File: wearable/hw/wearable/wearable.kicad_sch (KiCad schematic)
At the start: 104 parts, among them IC1 LM4041CILPR, J2 Conn_02x05_Odd_Even, J3 Interrupts, J4 Data, J5 Data, J8 USBC Charger, SW1 SW_Toggle, U1 LT3042xMSE, U2 BNO080, U3 nRF54L15-QFXX, U4 MAX77659AENV+, U5 ADS1299IPAG, U6 nPM1300-QEXX, Y1 32MHz, Y2 32.768kHz, Y3 32.768kHz

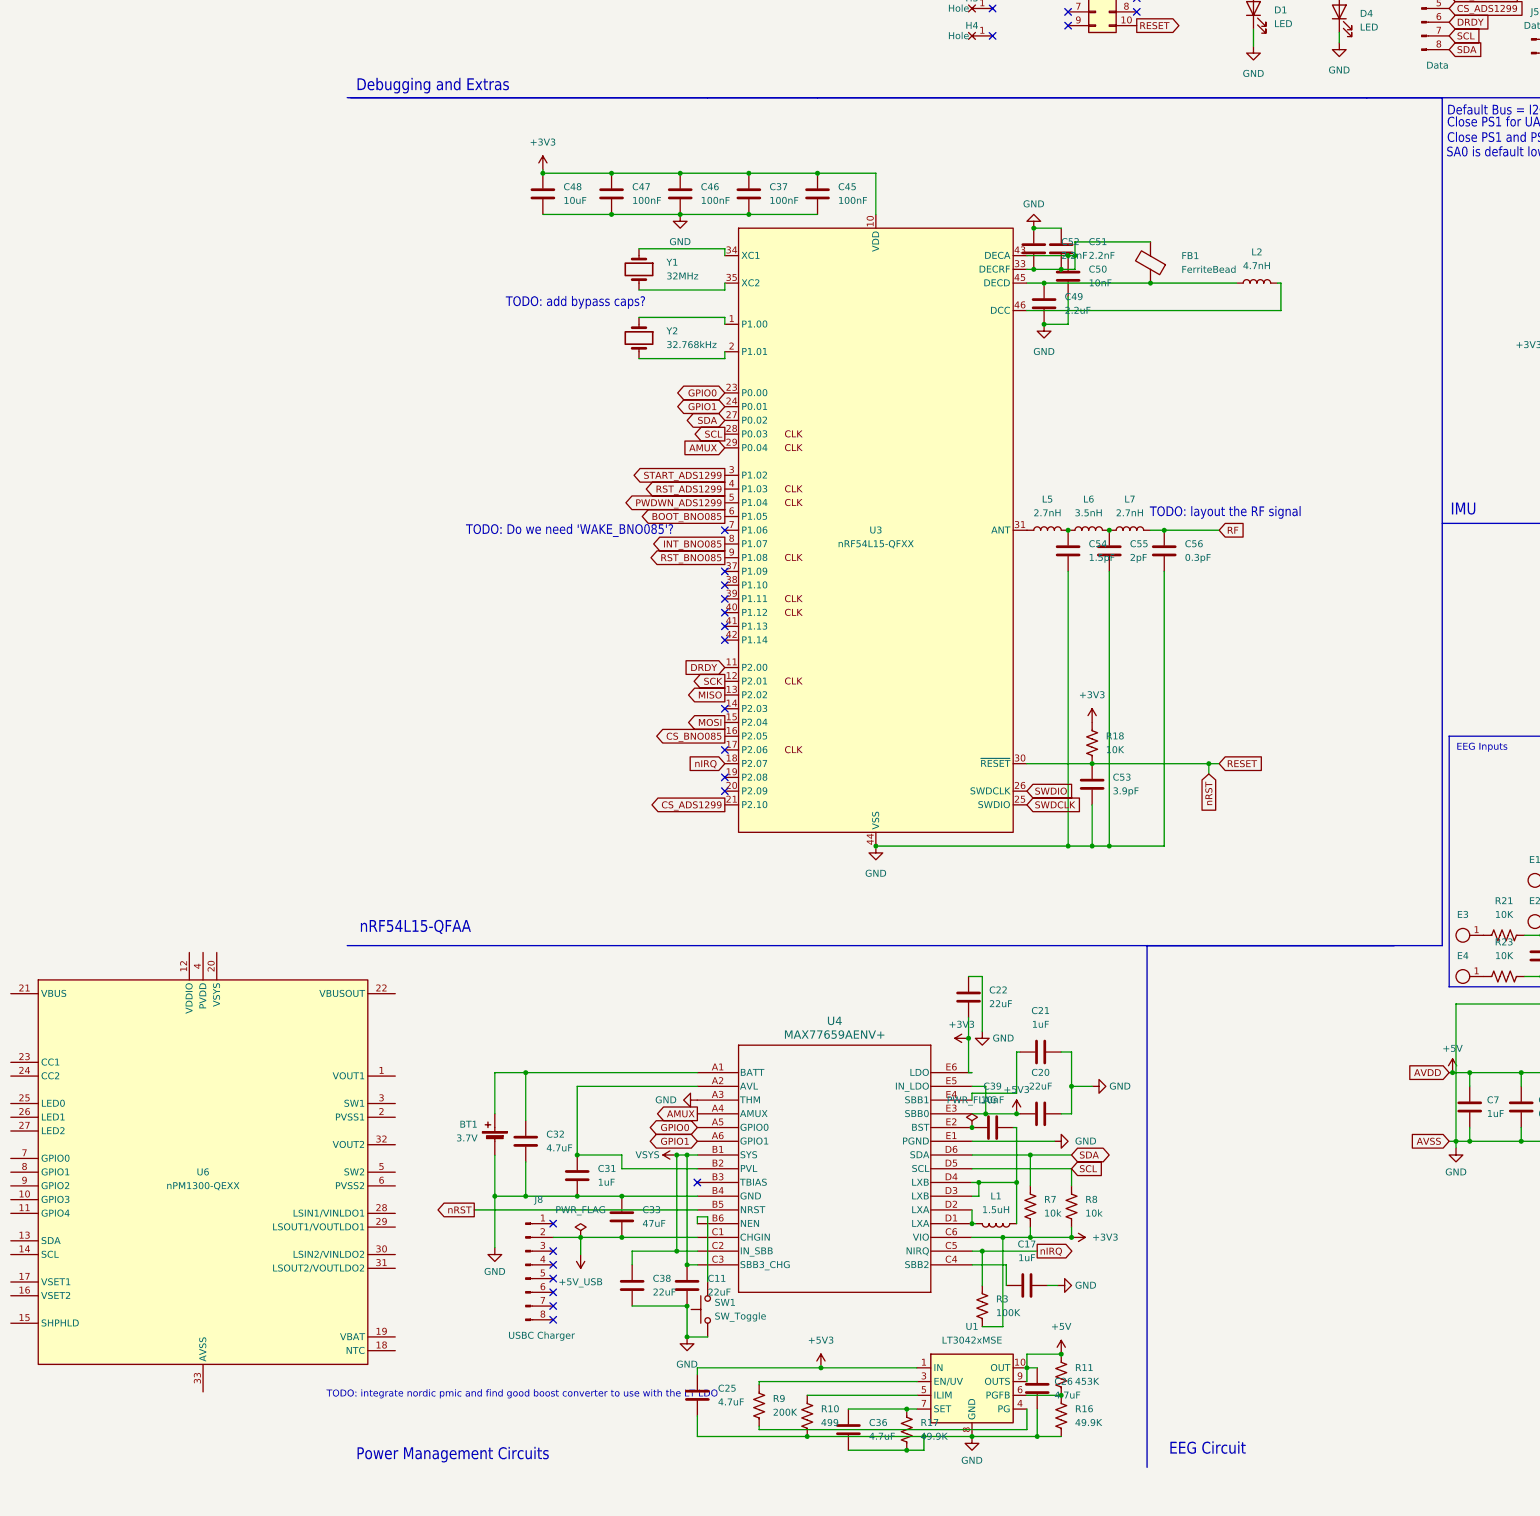
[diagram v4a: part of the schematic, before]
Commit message: Schematic of new power setup done
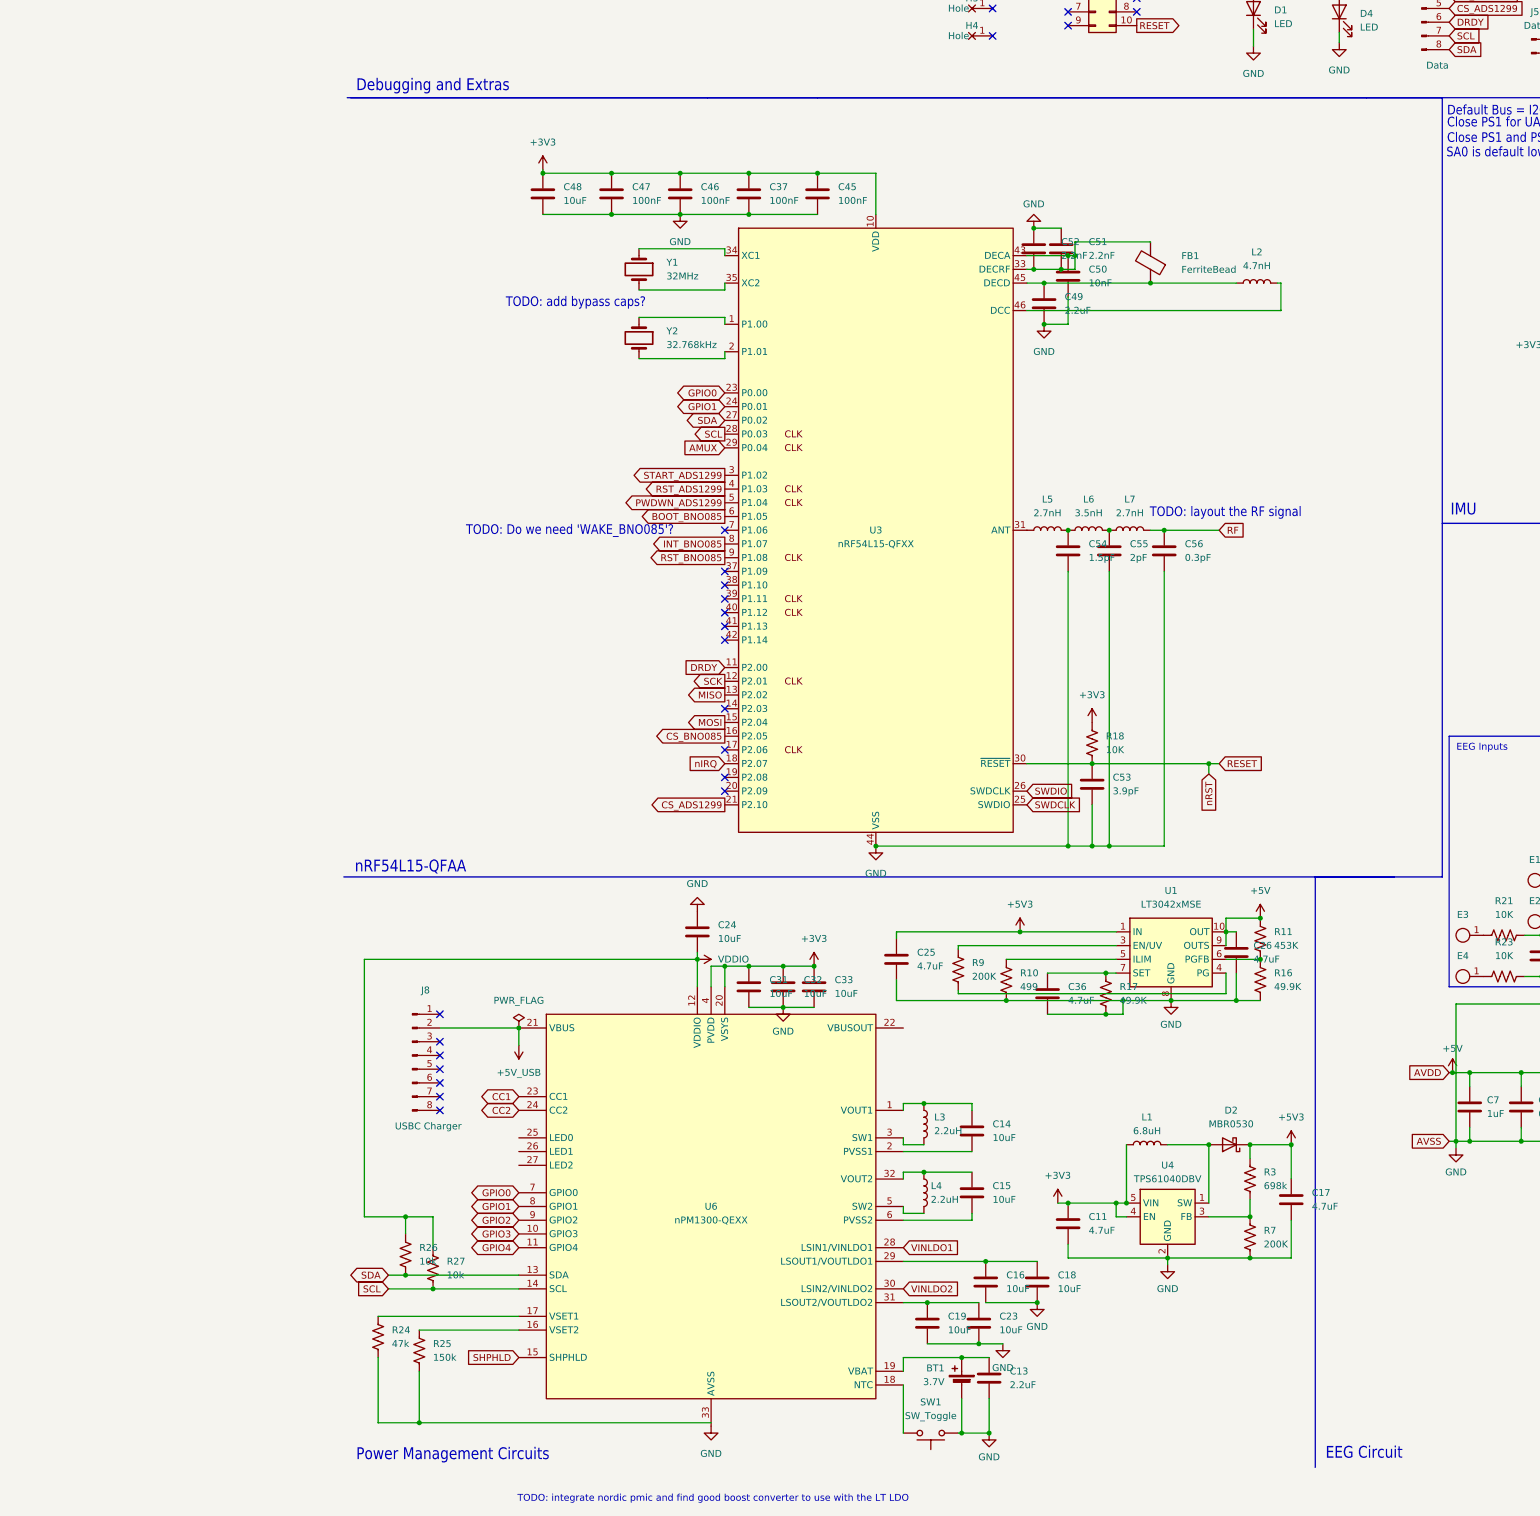
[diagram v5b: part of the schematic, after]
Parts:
- removed C20, C22, C38: 22uF, Capacitor_SMD:C_0402_1005Metric, symbol ECE445L:C
- removed C21: 1uF, Capacitor_SMD:C_0402_1005Metric, symbol ECE445L:C
- removed C39: 10nF, Capacitor_SMD:C_0402_1005Metric, symbol ECE445L:C
- removed R8: 10k, Resistor_SMD:R_0402_1005Metric, symbol Device:R_US
- removed U4: MAX77659AENV+, MAX77659AENV+:21-100509_N302D2&plus_1_MXM, symbol MAX77659:MAX77659AENV+
- added C13: 2.2uF, Capacitor_SMD:C_0402_1005Metric, symbol ECE445L:C
- added C14, C15, C16, C18, C19, C23, C24: 10uF, Capacitor_SMD:C_0402_1005Metric, symbol ECE445L:C
- added D2: MBR0530, Diode_SMD:D_SOD-123, symbol Diode:MBR0530
- added L3, L4: 2.2uH, Inductor_SMD:L_0402_1005Metric_Pad0.77x0.64mm_HandSolder, symbol Device:L
- added R24: 47k, Resistor_SMD:R_0402_1005Metric, symbol Device:R_US
- added R25: 150k, Resistor_SMD:R_0402_1005Metric, symbol Device:R_US
- added R26, R27: 10k, Resistor_SMD:R_0402_1005Metric, symbol Device:R_US
- added U4: TPS61040DBV, Package_TO_SOT_SMD:SOT-23-5, symbol Regulator_Switching:TPS61040DBV
- C11: value 22uF -> 4.7uF
- C17: value 1uF -> 4.7uF
- C31: value 1uF -> 10uF
- C32: value 4.7uF -> 10uF
- C33: value 47uF -> 10uF
- L1: value 1.5uH -> 6.8uH
- R3: value 100K -> 698k
- R7: value 10k -> 200K
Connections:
- net VSYS is gone; now on net +3V3: C11.1
- net +3V3: now also C31.1, C32.1, C33.1, L1.1, U6.20 (VSYS), U6.4 (PVDD), U4.4 (EN), U4.5 (VIN); no longer R3.2, R7.2
- net +5V3: now also C17.1, R3.1, D2.1 (K)
- net +5V_USB: now also U6.21 (VBUS); no longer C33.2
- net GND: now also C33.2, R7.2, U6.33 (AVSS), C13.2, C16.2, C18.2, C19.2, C23.2, C24.1, U4.2 (GND); no longer C33.1
- net GPIO0: now also U6.7 (GPIO0)
- net GPIO1: now also U6.8 (GPIO1)
- net SCL: now also U6.14 (SCL), R27.2
- net SDA: now also U6.13 (SDA), R26.2; no longer R7.1
- net nIRQ: no longer R3.1
- net at L1.2: now also D2.2 (A), U4.1 (SW)
- net at SW1.2: now also U6.18 (NTC)
- net at BT1.1 (+): now also U6.19 (VBAT), C13.1; no longer C32.1
- net at U6.1 (VOUT1): now also C14.1, L3.1
- net GPIO3: now reaches U6.10 (GPIO3)
- net GPIO4: now reaches U6.11 (GPIO4)
- net VDDIO: now reaches U6.12 (VDDIO)
- net VDDIO: now also C24.2, R26.1, R27.1
- net SHPHLD: now reaches U6.15 (SHPHLD)
- net at U6.16 (VSET2): now also R25.1
- net at U6.17 (VSET1): now also R24.1
- net at U6.2 (PVSS1): now also C14.2
- net CC1: now reaches U6.23 (CC1)
- net CC2: now reaches U6.24 (CC2)
- net VINLDO1: now reaches U6.28 (LSIN1/VINLDO1)
- net at U6.29 (LSOUT1/VOUTLDO1): now also C16.1, C18.1
- net at U6.3 (SW1): now also L3.2
- net VINLDO2: now reaches U6.30 (LSIN2/VINLDO2)
- net at U6.31 (LSOUT2/VOUTLDO2): now also C19.1, C23.1
- net at U6.32 (VOUT2): now also C15.1, L4.1
- net at U6.5 (SW2): now also L4.2
- net at U6.6 (PVSS2): now also C15.2
- net GPIO2: now reaches U6.9 (GPIO2)
- new net: R24.2, R25.2
- new net: R3.2, R7.1, U4.3 (FB)
- no-connect marks 34 -> 33
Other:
- moved on the sheet: BT1, C25, C26, C36, J8, R10, R11, R16, R17, R9, SW1, U1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

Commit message: Slop layout for new power block
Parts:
- added C20: 3.3pF, Capacitor_SMD:C_0402_1005Metric, symbol ECE445L:C
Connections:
- net +5V3: now also C20.1
- net GPIO0: now also U3.17 (P2.06); no longer U3.23 (P0.00)
- net GPIO1: now also U3.18 (P2.07); no longer U3.24 (P0.01)
- net GPIO2: now also U3.19 (P2.08)
- net GPIO3: now also U3.20 (P2.09)
- net GPIO4: now also U3.14 (P2.03)
- net at R3.2, R7.1, U4.3 (FB): now also C20.2
- net nIRQ: no longer names the net of J3.8 (Pin_8)
- net nIRQ: no longer U3.18 (P2.07)
- no-connect marks 33 -> 31
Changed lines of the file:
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@@
 	)
 	(junction
+		(at 169.545 237.49)
+		(diameter 0)
+		(color 0 0 0 0)
+	)
+	(junction
 		(at 139.7 213.36)
 		(diameter 0)
@@
 	)
 	(junction
+		(at 166.37 248.92)
+		(diameter 0)
+		(color 0 0 0 0)
+	)
+	(junction
 		(at 301.625 104.775)
 		(diameter 0)
@@
 	)
 	(no_connect
-		(at 69.215 164.465)
-	)
-	(no_connect
-		(at 69.215 156.845)
+		(at 299.085 81.915)
 	)
 	(no_connect
-		(at 299.085 81.915)
+		(at 69.215 100.965)
 	)
 	(no_connect
@@
 	)
 	(no_connect
+		(at 69.215 98.425)
+	)
+	(no_connect
 		(at 118.745 32.385)
 	)
@@
 	)
 	(no_connect
-		(at 69.215 172.085)
-	)
-	(no_connect
 		(at 16.51 223.52)
 	)
@@
 	)
 	(no_connect
-		(at 69.215 169.545)
-	)
-	(no_connect
 		(at 69.215 141.605)
 	)
@@
 	(wire
 		(pts
+			(xy 169.545 237.49) (xy 173.99 237.49)
+		)
+		(stroke
+			(width 0)
+			(type default)
+		)
+	)
+	(wire
+		(pts
 			(xy 229.87 206.375) (xy 229.87 201.295)
 		)
@@
 	(wire
 		(pts
+			(xy 169.545 237.49) (xy 169.545 241.3)
+		)
+		(stroke
+			(width 0)
+			(type default)
+		)
+	)
+	(wire
+		(pts
 			(xy 141.605 250.825) (xy 143.51 250.825)
 		)
@@
 	(wire
 		(pts
-			(xy 166.37 247.65) (xy 166.37 250.825)
+			(xy 166.37 247.65) (xy 166.37 248.92)
+		)
+		(stroke
+			(width 0)
+			(type default)
+		)
+	)
+	(wire
+		(pts
+			(xy 166.37 248.92) (xy 169.545 248.92)
 		)
 		(stroke
@@
 	(wire
 		(pts
-			(xy 166.37 237.49) (xy 173.99 237.49)
+			(xy 166.37 237.49) (xy 169.545 237.49)
 		)
 		(stroke
@@
 	(wire
 		(pts
+			(xy 166.37 248.92) (xy 166.37 250.825)
+		)
+		(stroke
+			(width 0)
+			(type default)
+		)
+	)
+	(wire
+		(pts
 			(xy 2.54 250.825) (xy 10.16 250.825)
 		)
@@
 		)
 	)
-	(global_label "GPIO1"
-		(shape bidirectional)
-		(at 69.215 100.965 180)
-		(fields_autoplaced yes)
-		(effects
-			(font
-				(size 1.27 1.27)
-			)
-			(justify right)
-		)
-		(property "Intersheetrefs" "${INTERSHEET_REFS}"
-			(at 59.4337 100.965 0)
-			(effects
-				(font
-					(size 1.27 1.27)
-				)
-				(justify right)
-				(hide yes)
-			)
-		)
-	)
 	(global_label "SDA"
 		(shape input)
@@
 		)
 	)
-	(global_label "GPIO0"
-		(shape bidirectional)
-		(at 69.215 98.425 180)
-		(fields_autoplaced yes)
-		(effects
-			(font
-				(size 1.27 1.27)
-			)
-			(justify right)
-		)
-		(property "Intersheetrefs" "${INTERSHEET_REFS}"
-			(at 59.4337 98.425 0)
-			(effects
-				(font
-					(size 1.27 1.27)
-				)
-				(justify right)
-				(hide yes)
-			)
-		)
-	)
 	(global_label "nRST"
 		(shape input)
@@
 		)
 	)
-	(global_label "nIRQ"
-		(shape input)
-		(at 69.215 167.005 180)
-		(fields_autoplaced yes)
-		(effects
-			(font
-				(size 1.27 1.27)
-			)
-			(justify right)
-		)
-		(property "Intersheetrefs" "${INTERSHEET_REFS}"
-			(at 61.8755 167.005 0)
-			(effects
-				(font
-					(size 1.27 1.27)
-				)
-				(justify right)
-				(hide yes)
-			)
-		)
-	)
 	(global_label "SCK"
 		(shape input)
@@
 		)
 	)
-	(global_label "nIRQ"
-		(shape input)
-		(at 240.03 35.56 0)
-		(fields_autoplaced yes)
-		(effects
-			(font
-				(size 1.27 1.27)
-			)
-			(justify left)
-		)
-		(property "Intersheetrefs" "${INTERSHEET_REFS}"
-			(at 247.3695 35.56 0)
-			(effects
-				(font
-					(size 1.27 1.27)
-				)
-				(justify left)
-				(hide yes)
-			)
-		)
-	)
 	(global_label "INT_BNO085"
 		(shape input)
@@
 		)
 	)
+	(global_label "GPIO0"
+		(shape bidirectional)
+		(at 69.215 164.465 180)
+		(fields_autoplaced yes)
+		(effects
+			(font
+				(size 1.27 1.27)
+			)
+			(justify right)
+		)
+		(property "Intersheetrefs" "${INTERSHEET_REFS}"
+			(at 59.4337 164.465 0)
+			(effects
+				(font
+					(size 1.27 1.27)
+				)
+				(justify right)
+				(hide yes)
+			)
+		)
+	)
 	(global_label "AMUX"
 		(shape input)
@@
 		)
 	)
+	(global_label "GPIO1"
+		(shape bidirectional)
+		(at 69.215 167.005 180)
+		(fields_autoplaced yes)
+		(effects
+			(font
+				(size 1.27 1.27)
+			)
+			(justify right)
+		)
+		(property "Intersheetrefs" "${INTERSHEET_REFS}"
+			(at 59.4337 167.005 0)
+			(effects
+				(font
+					(size 1.27 1.27)
+				)
+				(justify right)
+				(hide yes)
+			)
+		)
+	)
 	(global_label "GPIO4"
 		(shape bidirectional)
@@
 		)
 	)
+	(global_label "GPIO3"
+		(shape bidirectional)
+		(at 69.215 172.085 180)
+		(fields_autoplaced yes)
+		(effects
+			(font
+				(size 1.27 1.27)
+			)
+			(justify right)
+		)
+		(property "Intersheetrefs" "${INTERSHEET_REFS}"
+			(at 59.4337 172.085 0)
+			(effects
+				(font
+					(size 1.27 1.27)
+				)
+				(justify right)
+				(hide yes)
+			)
+		)
+	)
+	(global_label "GPIO4"
+		(shape bidirectional)
+		(at 69.215 156.845 180)
+		(fields_autoplaced yes)
+		(effects
+			(font
+				(size 1.27 1.27)
+			)
+			(justify right)
+		)
+		(property "Intersheetrefs" "${INTERSHEET_REFS}"
+			(at 59.4337 156.845 0)
+			(effects
+				(font
+					(size 1.27 1.27)
+				)
+				(justify right)
+				(hide yes)
+			)
+		)
+	)
 	(global_label "GPIO0"
 		(shape input)
@@
 		)
 	)
+	(global_label "GPIO2"
+		(shape bidirectional)
+		(at 69.215 169.545 180)
+		(fields_autoplaced yes)
+		(effects
+			(font
+				(size 1.27 1.27)
+			)
+			(justify right)
+		)
+		(property "Intersheetrefs" "${INTERSHEET_REFS}"
+			(at 59.4337 169.545 0)
+			(effects
+				(font
+					(size 1.27 1.27)
+				)
+				(justify right)
+				(hide yes)
+			)
+		)
+	)
 	(global_label "PWDWN_ADS1299"
 		(shape input)
@@
 					(unit 1)
 				)
+			)
+		)
+	)
+	(symbol
+		(lib_id "ECE445L:C")
+		(at 169.545 245.11 0)
+		(unit 1)
+		(exclude_from_sim no)
+		(in_bom yes)
+		(on_board yes)
+		(dnp no)
+		(property "Reference" "C20"
+			(at 173.355 243.8399 0)
+			(effects
+				(font
+					(size 1.27 1.27)
+				)
+				(justify left)
+			)
+		)
+		(property "Value" "3.3pF"
+			(at 173.355 246.3799 0)
+			(effects
+				(font
+					(size 1.27 1.27)
+				)
+				(justify left)
+			)
+		)
+		(property "Footprint" "Capacitor_SMD:C_0402_1005Metric"
+			(at 170.5102 248.92 0)
+			(effects
+				(font
+					(size 1.27 1.27)
+				)
+				(hide yes)
+			)
+		)
+		(property "Datasheet" "~"
+			(at 169.545 245.11 0)
+			(effects
+				(font
+					(size 1.27 1.27)
+				)
+				(hide yes)
+			)
+		)
+		(property "Description" "Unpolarized capacitor"
+			(at 169.545 245.11 0)
+			(effects
+				(font
+					(size 1.27 1.27)
+				)
+				(hide yes)
+			)
+		)
+		(pin "1"
+		)
+		(pin "2"
+		)
+		(instances
+			(project "wearable"
+				(path "/eeafcd59-7fa6-43d8-bb03-b6b192c7124f"
+					(reference "C20")
+					(unit 1)
+				)

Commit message: Questioning life choices
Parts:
- removed J3: Interrupts, Connector_PinHeader_1.00mm:PinHeader_1x08_P1.00mm_Vertical, symbol ECE445L:Conn_01x08_Pin
- removed J4: Data, Connector_PinHeader_1.00mm:PinHeader_1x08_P1.00mm_Vertical, symbol ECE445L:Conn_01x08_Pin
- removed J5: Data, Connector_PinHeader_1.00mm:PinHeader_1x02_P1.00mm_Vertical, symbol Connector:Conn_01x02_Pin
- removed TP3: BatteryStatus, TestPoint:TestPoint_Bridge_Pitch2.0mm_Drill0.7mm, symbol Connector:TestPoint
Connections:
- net CS_BNO085: now also U3.20 (P2.09); no longer U3.16 (P2.05)
- net GPIO0: now also U3.15 (P2.04); no longer U3.17 (P2.06)
- net GPIO1: now also U3.16 (P2.05); no longer U3.18 (P2.07)
- net GPIO2: now also U3.17 (P2.06); no longer U3.19 (P2.08)
- net GPIO3: now also U3.18 (P2.07); no longer U3.20 (P2.09)
- net GPIO4: now also U3.19 (P2.08); no longer U3.14 (P2.03)
- net MOSI: now also U3.14 (P2.03); no longer U3.15 (P2.04)
- net AMUX: no longer names the net of U3.29 (P0.04)
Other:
- moved on the sheet: TP1, TP2
